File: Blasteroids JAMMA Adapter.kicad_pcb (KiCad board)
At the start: 2 copper layers, 112.2 x 82 mm, 49 parts, among them P1 10K, U1 74LS86, U2 NE555, U3 MC34063AP, U4 LM386, U5 NE555

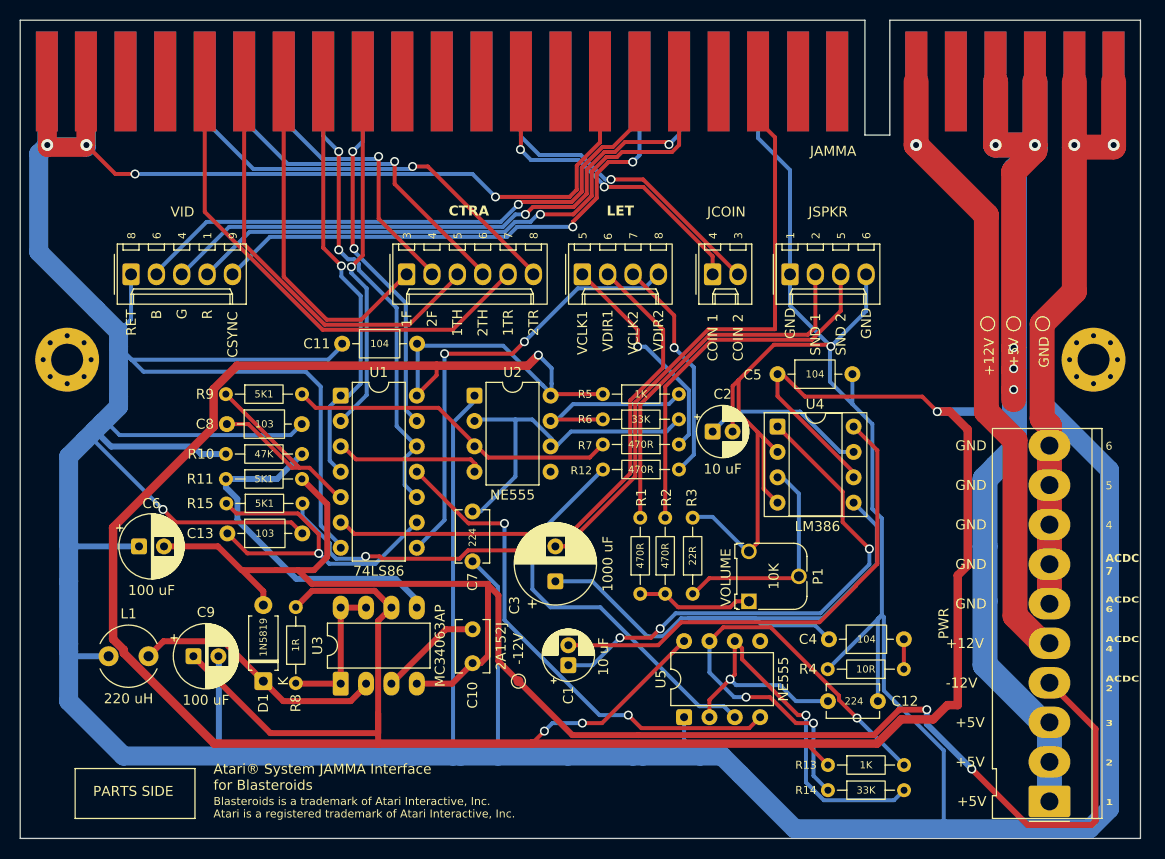
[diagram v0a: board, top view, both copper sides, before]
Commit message: improve decoupling, cleanup trace
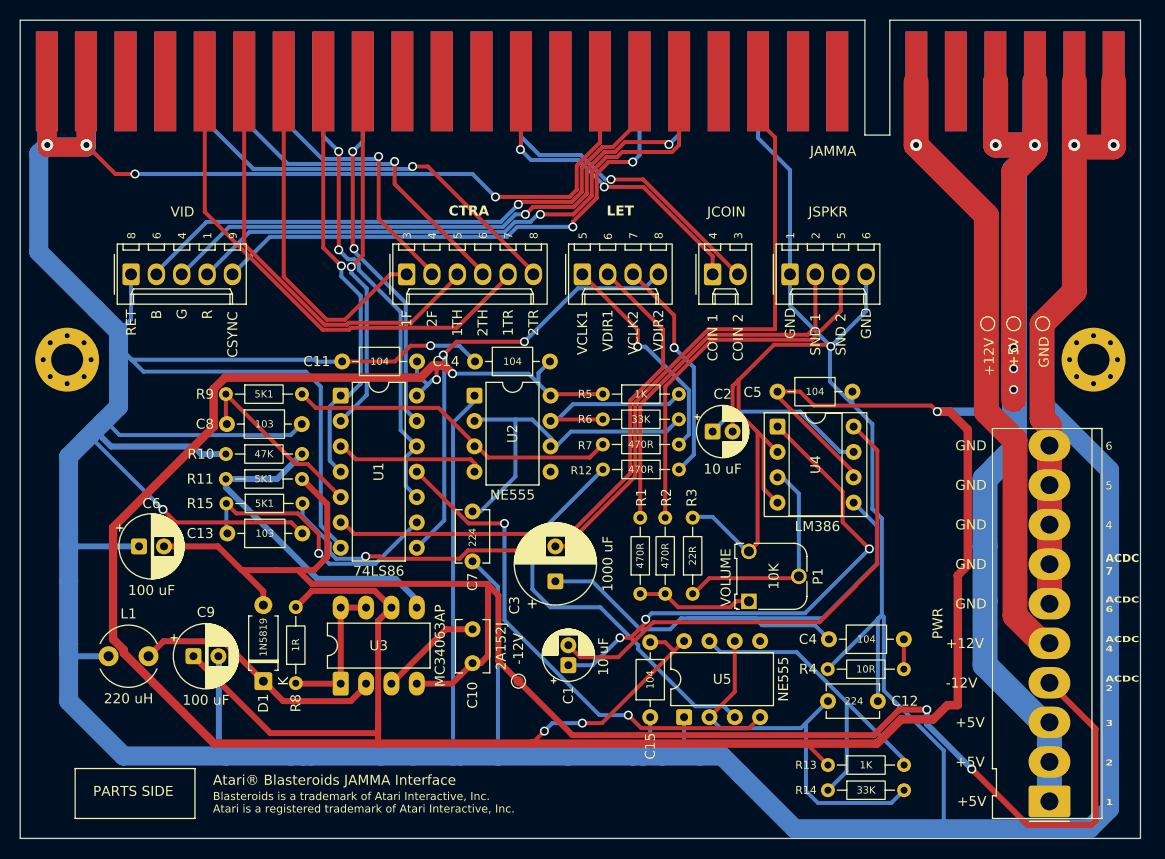
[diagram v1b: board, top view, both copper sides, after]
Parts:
- added C14: 104, Capacitor_THT:C_Axial_L3.8mm_D2.6mm_P7.50mm_Horizontal, F.Cu at (134.5, 79.0)
- added C15: 104, Capacitor_THT:C_Axial_L3.8mm_D2.6mm_P7.50mm_Horizontal, F.Cu at (152.0, 114.6)
- moved C11 1.78 mm to (121.1, 79.0)
- moved C5 1.75 mm to (164.8, 82.0)
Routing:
- net +5V: track 465.9 -> 448.5 mm, vias 9 -> 10
- net GND: track 797.8 -> 814.4 mm, vias 8 -> 9
- net U5_DIS: track 49.0 -> 34.5 mm, vias 3 -> 0
- net U5_THR: track 48.1 -> 39.8 mm, vias 2 -> 0
- net VCLK2_DELAYED: track 34.4 -> 27.5 mm
- net VCLK1_DELAYED: track 24.9 -> 18.8 mm
- net CINV_R10_R9: track 35.3 -> 34.1 mm
- net U4_GAIN_P8: track 49.1 -> 50.1 mm
- net U4_GAIN_P1: track 51.9 -> 51.2 mm
- net AUDIO_PREAMP_OUT: track 59.6 -> 59.0 mm
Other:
- board text added: "Atari® Blasteroids JAMMA Interface"
- board text removed: "Atari® System JAMMA Interface for Blasteroids"
